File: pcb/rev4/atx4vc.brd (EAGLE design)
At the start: 69 x 69 mm, 58 parts, among them IC1 MY_7905DT, IC2 MAX486X/SOT, J2 ATX24RH

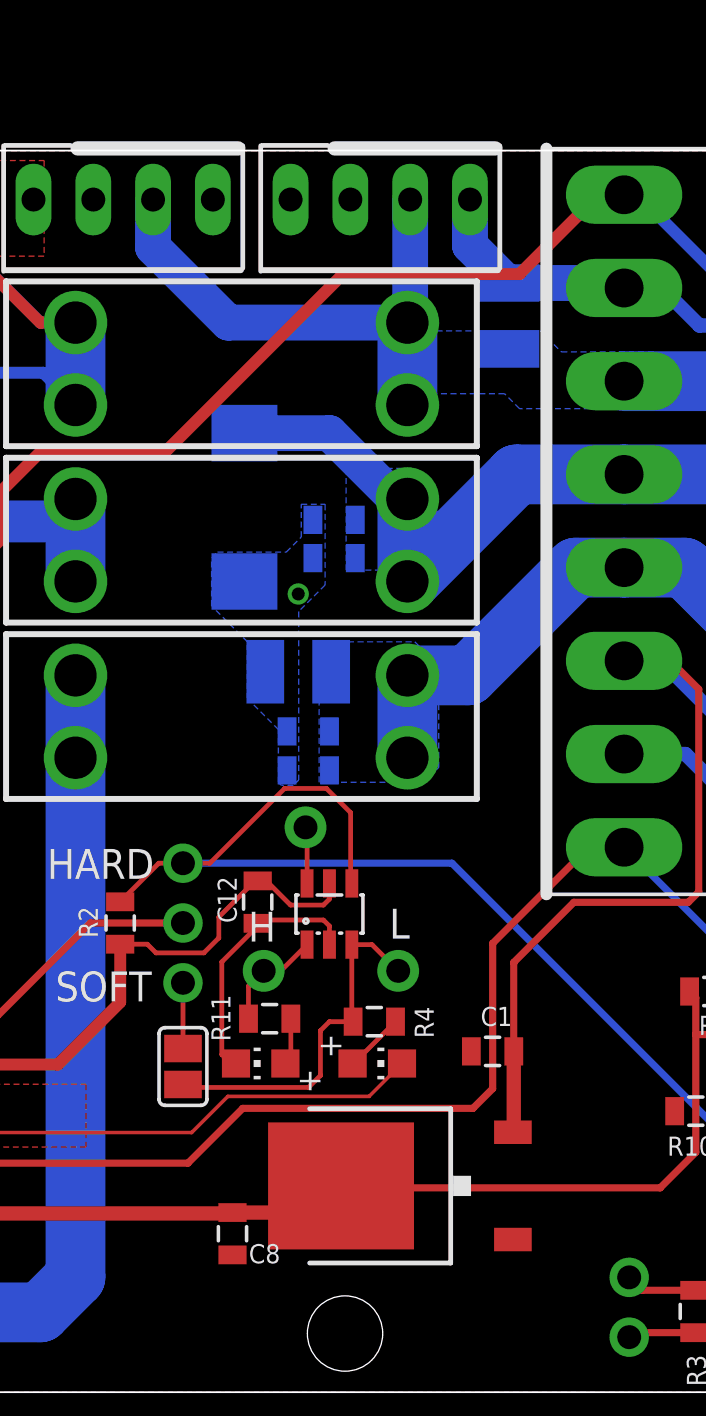
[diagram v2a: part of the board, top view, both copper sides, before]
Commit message: trying out power ic
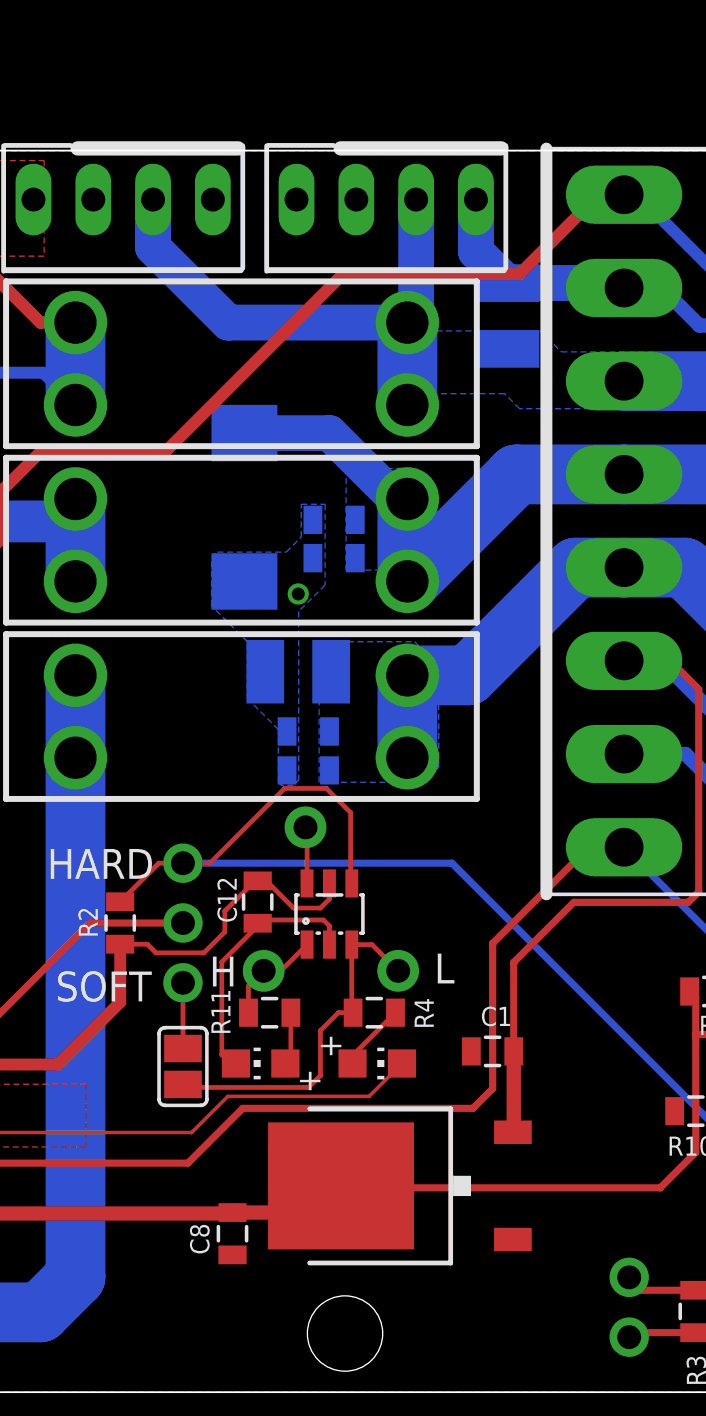
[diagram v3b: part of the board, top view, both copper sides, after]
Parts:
- moved R4 0.38 mm to (35.6, 24.1)
- moved JP5 0.25 mm to (36.1, 58.7)
- moved R11 0.25 mm to (31.1, 24.1)
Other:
- board text removed: "DM"
- board text removed: "DP"
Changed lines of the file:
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@@
 <text x="88.9085" y="73.703" size="1.6764" layer="25" align="center">MAKE SURE TO USE
 12V RATED CAPS ON 12V LINES</text>
-<text x="65.8575" y="44.839" size="2.54" layer="26" rot="MR270" align="center">+</text>
 <text x="41.2815" y="50.43" size="1.27" layer="26" rot="MR0" align="center">12</text>
 <text x="28.3925" y="47.76" size="2.1844" layer="26" rot="MR0">+</text>
@@
 <dimension x1="4.0655" y1="65" x2="4.0655" y2="4" x3="-12.0825" y3="34.5" textsize="1.778" layer="51" dtype="vertical"/>
 <dimension x1="65.0655" y1="65" x2="65.0655" y2="4" x3="94.5175" y3="34.5" textsize="1.778" layer="51" dtype="vertical"/>
-<text x="55.5765" y="12.227" size="1.27" layer="26" rot="MR0" align="center">DP</text>
-<text x="55.5765" y="10.4" size="1.27" layer="26" rot="MR0" align="center">DM</text>
 <text x="30.0175" y="46.4" size="1.6764" layer="26" rot="MR0" align="center">5V</text>
 <text x="35.5185" y="21.23" size="3.175" layer="26" ratio="10" rot="MR0" align="center">ATX4VC.com</text>
@@
 <text x="63.0635" y="21.979" size="2.1844" layer="26" rot="MR180" align="center">PG</text>
 <text x="63.1905" y="42.045" size="2.1844" layer="26" rot="MR180" align="center">+5</text>
-<text x="30.791" y="27.7845" size="1.27" layer="25" rot="R180" align="center">H</text>
-<text x="36.633" y="27.9115" size="1.27" layer="25" rot="R180" align="center">L</text>
+<text x="29.14" y="25.8795" size="1.27" layer="25" rot="R180" align="center">H</text>
+<text x="38.538" y="26.0065" size="1.27" layer="25" rot="R180" align="center">L</text>
 <text x="24.06" y="25.2445" size="1.27" layer="25" rot="R180" align="center">SOFT</text>
 <text x="23.933" y="30.4515" size="1.27" layer="25" rot="R180" align="center">HARD</text>
@@
 <element name="U$7" library="atx4vc" package="396_CONN_396_8P" value="396_CONN_VH396_8P" x="46.1725" y="43.038" smashed="yes" rot="R90"/>
 <element name="U$12" library="atx4vc" package="DG2204R-8" value="DG2204R-5.0-8DG2204-8" x="63.0635" y="42.045" smashed="yes" rot="R270"/>
-<element name="JP5" library="appleii" package="1X04" value="" x="35.814" y="58.674" smashed="yes" rot="R180"/>
+<element name="JP5" library="appleii" package="1X04" value="" x="36.068" y="58.674" smashed="yes" rot="R180"/>
 <element name="J1" library="SparkFun-Connectors" package="USB-C-16P" value="" x="61.3485" y="13.089" smashed="yes" rot="R90">
 <attribute name="PROD_ID" value="CONN-14122" x="61.0945" y="13.089" size="1.778" layer="27" rot="R90" display="off"/>
@@
 </element>
 <element name="C8" library="atx_power_control" package="0805$1" value="2.2uF" x="29.5355" y="14.74" smashed="yes" rot="R90">
-<attribute name="NAME" x="31.5675" y="14.2955" size="0.8128" layer="25" rot="R180"/>
+<attribute name="NAME" x="27.7415" y="15.1845" size="0.8128" layer="25" rot="R270"/>
 </element>
 <element name="C27" library="clock" package="C1210" value="47uF" x="32.3295" y="38.616" smashed="yes" rot="MR0">
@@
 <attribute name="NAME" x="23.8125" y="27.305" size="0.8128" layer="25" rot="R90"/>
 </element>
-<element name="R4" library="atx_power_control" package="0805" value="5K1" x="35.56" y="23.749" smashed="yes" rot="R180">
-<attribute name="NAME" x="37.2745" y="24.384" size="0.8128" layer="25" rot="R270"/>
+<element name="R4" library="atx_power_control" package="0805" value="5K1" x="35.56" y="24.13" smashed="yes" rot="R180">
+<attribute name="NAME" x="37.2745" y="24.765" size="0.8128" layer="25" rot="R270"/>
 </element>
 <element name="LED8" library="adafruit" package="CHIP-LED0805" value="" x="35.687" y="21.971" smashed="yes" rot="R270">
 <attribute name="VALUE" x="34.417" y="19.431" size="1.27" layer="27"/>
 </element>
-<element name="R11" library="atx_power_control" package="0805" value="5K1" x="31.115" y="23.876" smashed="yes" rot="R180">
-<attribute name="NAME" x="28.6385" y="24.892" size="0.8128" layer="25" rot="R270"/>
+<element name="R11" library="atx_power_control" package="0805" value="5K1" x="31.115" y="24.13" smashed="yes" rot="R180">
+<attribute name="NAME" x="28.6385" y="25.146" size="0.8128" layer="25" rot="R270"/>
 </element>
 <element name="LED9" library="adafruit" package="CHIP-LED0805" value="" x="30.734" y="21.971" smashed="yes" rot="R90">
@@
 <wire x1="45.9615" y1="55.129" x2="41.2195" y2="55.129" width="1.524" layer="16"/>
 <contactref element="JP1" pad="1"/>
-<wire x1="39.624" y1="56.7245" x2="39.624" y2="58.674" width="1.524" layer="16"/>
-<wire x1="41.2195" y1="55.129" x2="39.624" y2="56.7245" width="1.524" layer="16"/>
+<wire x1="39.878" y1="56.4705" x2="39.878" y2="58.674" width="1.524" layer="16"/>
+<wire x1="41.2195" y1="55.129" x2="39.878" y2="56.4705" width="1.524" layer="16"/>
 <contactref element="IC2" pad="2"/>
 <contactref element="C12" pad="1"/>
@@
 <wire x1="26.289" y1="26.67" x2="28.321" y2="26.67" width="0.2032" layer="1"/>
 <wire x1="26.289" y1="26.67" x2="25.919" y2="27.04" width="0.2032" layer="1"/>
-<wire x1="28.321" y1="26.67" x2="28.956" y2="27.305" width="0.2032" layer="1"/>
-<wire x1="28.956" y1="27.305" x2="28.956" y2="28.194" width="0.2032" layer="1"/>
-<wire x1="28.956" y1="28.194" x2="30.491" y2="29.729" width="0.2032" layer="1"/>
+<wire x1="28.321" y1="26.67" x2="29.21" y2="27.559" width="0.2032" layer="1"/>
+<wire x1="29.21" y1="27.559" x2="29.21" y2="28.448" width="0.2032" layer="1"/>
+<wire x1="29.21" y1="28.448" x2="30.491" y2="29.729" width="0.2032" layer="1"/>
 <wire x1="30.491" y1="29.729" x2="30.607" y2="29.729" width="0.2032" layer="1"/>
-<wire x1="33.655" y1="28.956" x2="33.401" y2="28.702" width="0.2032" layer="1"/>
-<wire x1="33.401" y1="28.702" x2="32.004" y2="28.702" width="0.2032" layer="1"/>
+<wire x1="33.655" y1="28.956" x2="33.274" y2="28.575" width="0.2032" layer="1"/>
+<wire x1="33.274" y1="28.575" x2="32.131" y2="28.575" width="0.2032" layer="1"/>
 <wire x1="30.977" y1="29.729" x2="30.607" y2="29.729" width="0.2032" layer="1"/>
-<wire x1="32.004" y1="28.702" x2="30.977" y2="29.729" width="0.2032" layer="1"/>
+<wire x1="32.131" y1="28.575" x2="30.977" y2="29.729" width="0.2032" layer="1"/>
 <wire x1="33.655" y1="29.621" x2="33.655" y2="28.956" width="0.2032" layer="1"/>
 </signal>
@@
 <wire x1="50.3975" y1="50.958" x2="46.1725" y2="50.958" width="0.2032" layer="16"/>
 <contactref element="C11" pad="1"/>
-<wire x1="37.16339375" y1="53.64389375" x2="36.9665" y2="53.447" width="1.524" layer="16"/>
 <polygon width="0.1524" layer="16" thermals="no">
 <vertex x="42.6165" y="53.094"/>
@@
 </polygon>
 <contactref element="JP1" pad="2"/>
-<wire x1="37.084" y1="58.674" x2="37.084" y2="53.7232875" width="1.524" layer="16"/>
-<wire x1="37.084" y1="53.7232875" x2="37.16339375" y2="53.64389375" width="1.524" layer="16"/>
+<wire x1="37.338" y1="58.674" x2="37.338" y2="53.8185" width="1.524" layer="16"/>
+<wire x1="36.9665" y1="53.447" x2="37.338" y2="53.8185" width="1.524" layer="16"/>
 <wire x1="36.9665" y1="53.447" x2="29.357" y2="53.447" width="1.524" layer="16"/>
 <wire x1="26.162" y1="56.642" x2="26.162" y2="58.674" width="1.524" layer="16"/>
@@
 <wire x1="31.592" y1="25.908" x2="30.861" y2="25.908" width="0.2032" layer="1"/>
 <wire x1="30.861" y1="25.908" x2="30.215" y2="25.262" width="0.2032" layer="1"/>
-<wire x1="30.215" y1="25.262" x2="30.215" y2="23.876" width="0.2032" layer="1"/>
+<wire x1="30.215" y1="25.262" x2="30.215" y2="24.13" width="0.2032" layer="1"/>
 </signal>
 <signal name="N$12">
@@
 <contactref element="R4" pad="1"/>
 <contactref element="LED8" pad="A"/>
-<wire x1="36.46" y1="23.749" x2="34.682" y2="21.971" width="0.2032" layer="1"/>
-<wire x1="34.682" y1="21.971" x2="34.637" y2="21.971" width="0.2032" layer="1"/>
+<wire x1="36.46" y1="24.13" x2="34.637" y2="22.307" width="0.2032" layer="1"/>
+<wire x1="34.637" y1="21.971" x2="34.637" y2="22.307" width="0.2032" layer="1"/>
 </signal>
 <signal name="N$16">
 <contactref element="R11" pad="1"/>
 <contactref element="LED9" pad="A"/>
-<wire x1="32.015" y1="23.876" x2="32.015" y2="22.202" width="0.2032" layer="1"/>
+<wire x1="32.015" y1="24.13" x2="32.015" y2="22.202" width="0.2032" layer="1"/>
 <wire x1="32.015" y1="22.202" x2="31.784" y2="21.971" width="0.2032" layer="1"/>
 </signal>
@@
 <contactref element="JP8" pad="1"/>
 <contactref element="SJ1" pad="2"/>
-<wire x1="34.605" y1="27.021" x2="34.605" y2="23.804" width="0.2032" layer="1"/>
-<wire x1="34.605" y1="23.804" x2="34.66" y2="23.749" width="0.2032" layer="1"/>
-<wire x1="34.66" y1="23.749" x2="33.655" y2="23.749" width="0.2032" layer="1"/>
+<wire x1="34.605" y1="27.021" x2="34.605" y2="24.185" width="0.2032" layer="1"/>
+<wire x1="34.605" y1="24.185" x2="34.66" y2="24.13" width="0.2032" layer="1"/>
+<wire x1="34.66" y1="24.13" x2="34.036" y2="24.13" width="0.2032" layer="1"/>
 <wire x1="33.274" y1="23.368" x2="33.274" y2="21.463" width="0.2032" layer="1"/>
 <wire x1="33.274" y1="21.463" x2="32.766" y2="20.955" width="0.2032" layer="1"/>
 <wire x1="32.766" y1="20.955" x2="27.559" y2="20.955" width="0.2032" layer="1"/>
 <wire x1="27.559" y1="20.955" x2="27.432" y2="21.082" width="0.2032" layer="1"/>
-<wire x1="33.655" y1="23.749" x2="33.274" y2="23.368" width="0.2032" layer="1"/>
+<wire x1="34.036" y1="24.13" x2="33.274" y2="23.368" width="0.2032" layer="1"/>
 <wire x1="34.605" y1="27.021" x2="35.463" y2="27.021" width="0.2032" layer="1"/>
 <wire x1="35.463" y1="27.021" x2="36.576" y2="25.908" width="0.2032" layer="1"/>

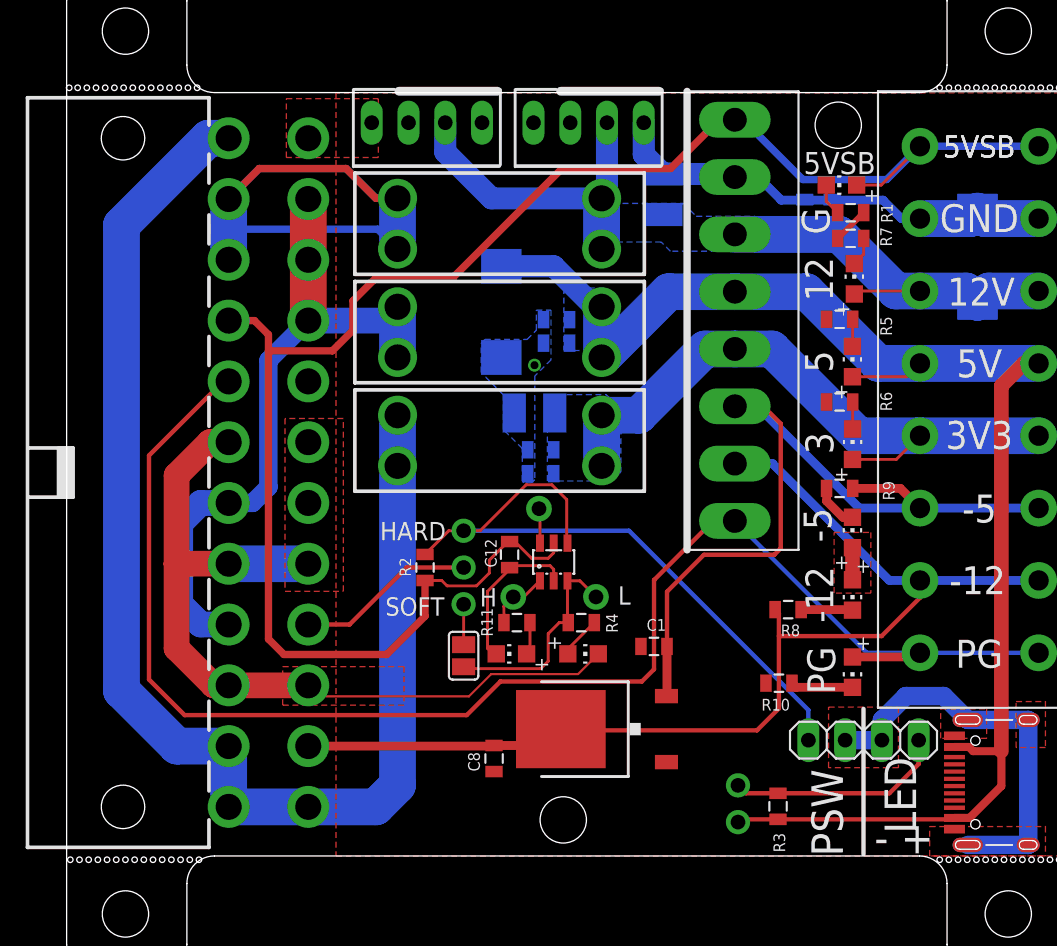
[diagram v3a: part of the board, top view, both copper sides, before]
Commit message: soft power ic tested working
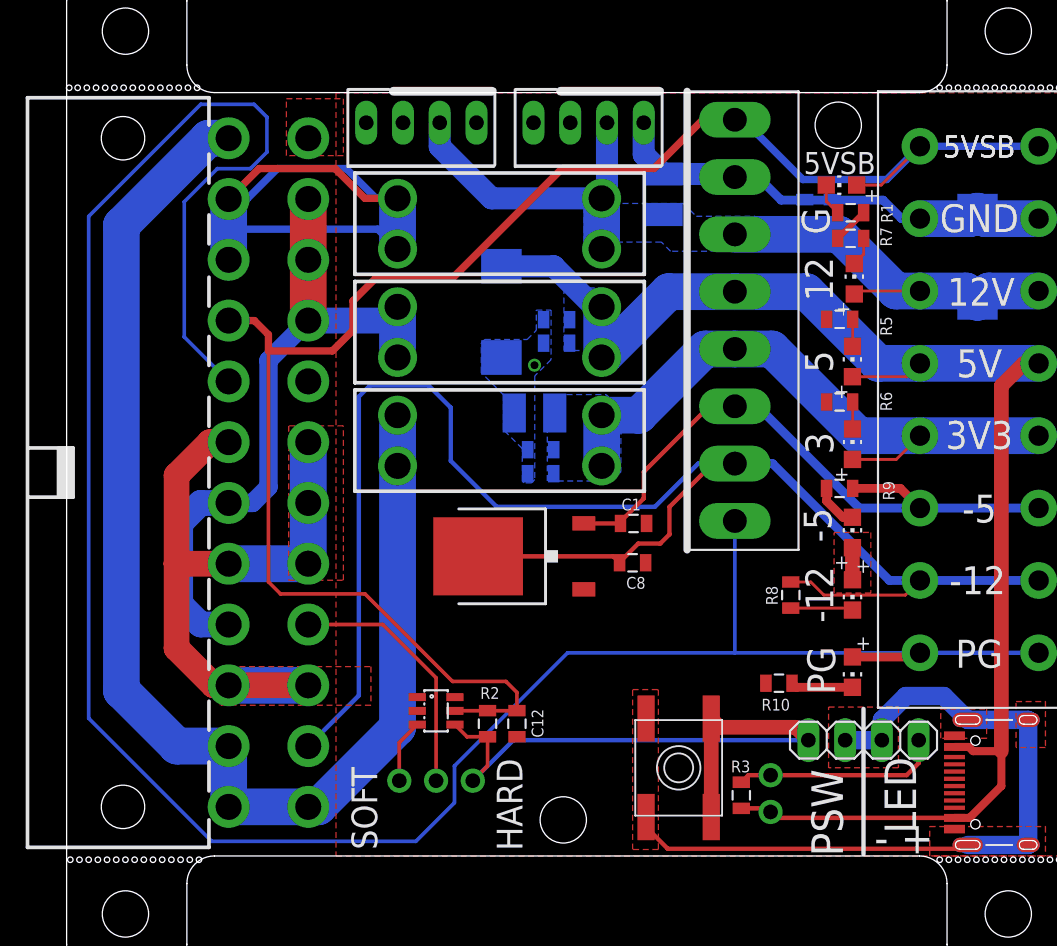
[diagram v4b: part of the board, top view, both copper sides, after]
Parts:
- removed JP3, JP6, JP8: (no value), adafruit_changed:1X01-CLEANBIG
- removed LED8, LED9: (no value), adafruit:CHIP-LED0805
- removed R11, R4: 5K1, atx_power_control:0805
- removed SJ1: (no value), jumper:SJ
- added SW1: SPST_TACT-EVQQ2, duckypad:EVQ-Q2
- moved C8 16.6 mm to (39.1, 28.3), turned to 180 degrees
- moved JP7 14.9 mm to (25.5, 13.2), turned to 0 degrees
- moved IC1 13.2 mm to (30.9, 28.7)
- moved IC2 13.1 mm to (25.5, 18.0), turned to 270 degrees
- moved C12 11.7 mm to (31.1, 17.1)
- moved R2 11.6 mm to (29.1, 17.1), turned to 270 degrees
- moved C1 8.61 mm to (39.2, 31.0), turned to 180 degrees
- moved R3 2.65 mm to (46.6, 12.2)
- moved U$13 2.36 mm to (48.6, 12.3)
- moved R8 1.02 mm to (50.0, 26.0), turned to 270 degrees
- moved JP1 0.38 mm to (24.5, 58.7)
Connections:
- removed net N$13: LED8.A, R4.1
- removed net N$16: LED9.A, R11.1
- removed net N$19: IC2.3, JP8.1, R4.2, SJ1.2
- removed net N$3: IC2.6, JP3.1
- removed net N$7: IC2.1, JP6.1, R11.2
- net GND: now also SW1.B, SW1.B'; no longer LED8.C, LED9.C
- net N$12: now also SW1.A, SW1.A'
- net N$6: now also IC2.3; no longer SJ1.1
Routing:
- net N$11: track 103.3 -> 164.1 mm
- net -12V: track 77.0 -> 114.7 mm
- net N$19: track 15.1 -> 0.00 mm
- net -5V: track 57.7 -> 44.1 mm
- net N$15: track 12.4 -> 17.5 mm
- net VCC: track 120.3 -> 115.3 mm
- net GND: track 136.6 -> 141.6 mm
- net N$7: track 4.35 -> 0.00 mm
- net N$13: track 2.91 -> 0.00 mm
- net N$3: track 2.41 -> 0.00 mm
- net N$14: track 93.1 -> 90.8 mm
- net N$16: track 2.25 -> 0.00 mm
- net N$12: track 46.3 -> 44.5 mm
- net N$6: track 2.79 -> 4.39 mm
- net N$8: track 3.56 -> 4.32 mm
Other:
- board text added: "header as switch 5mm from edge"
- board text removed: "H"
- board text removed: "L"
